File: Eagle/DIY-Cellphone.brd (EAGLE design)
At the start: 87 x 44.5 mm, 47 parts, among them IC1 MEGA1284, J1 ISP, U1 MCP73831, U7 M10_HDWITHOUT_EXCLUSION, X1 BU-SMA-V, X3 CCM03-3002 R102

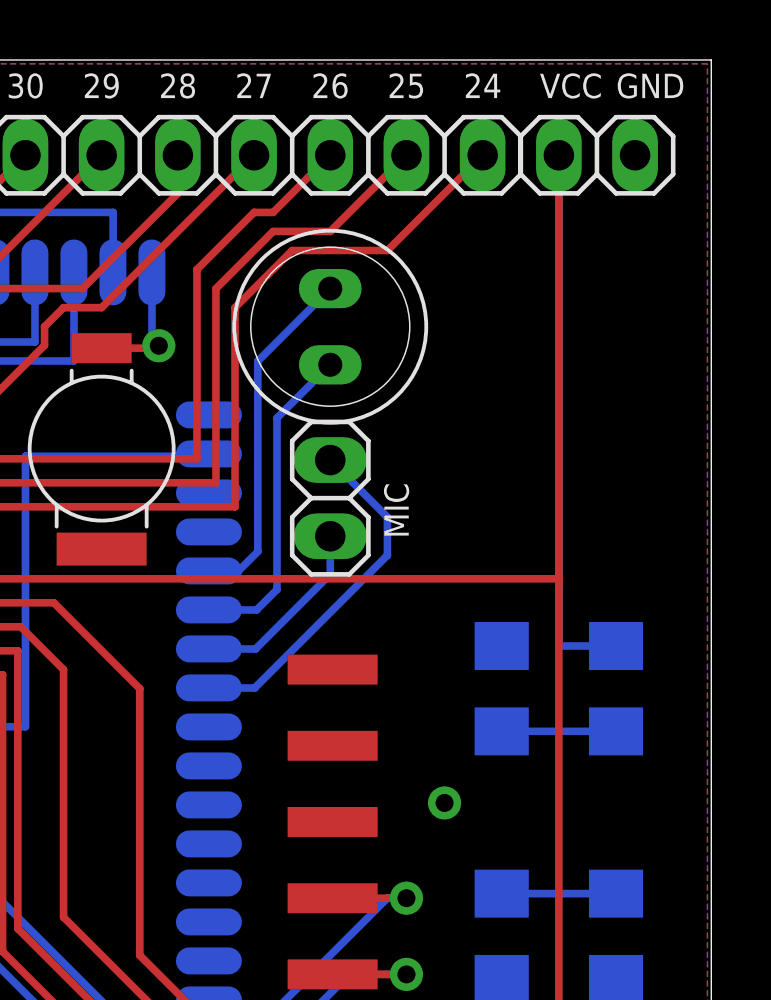
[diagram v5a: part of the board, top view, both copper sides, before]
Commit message: Move speaker and mic to edge of board.
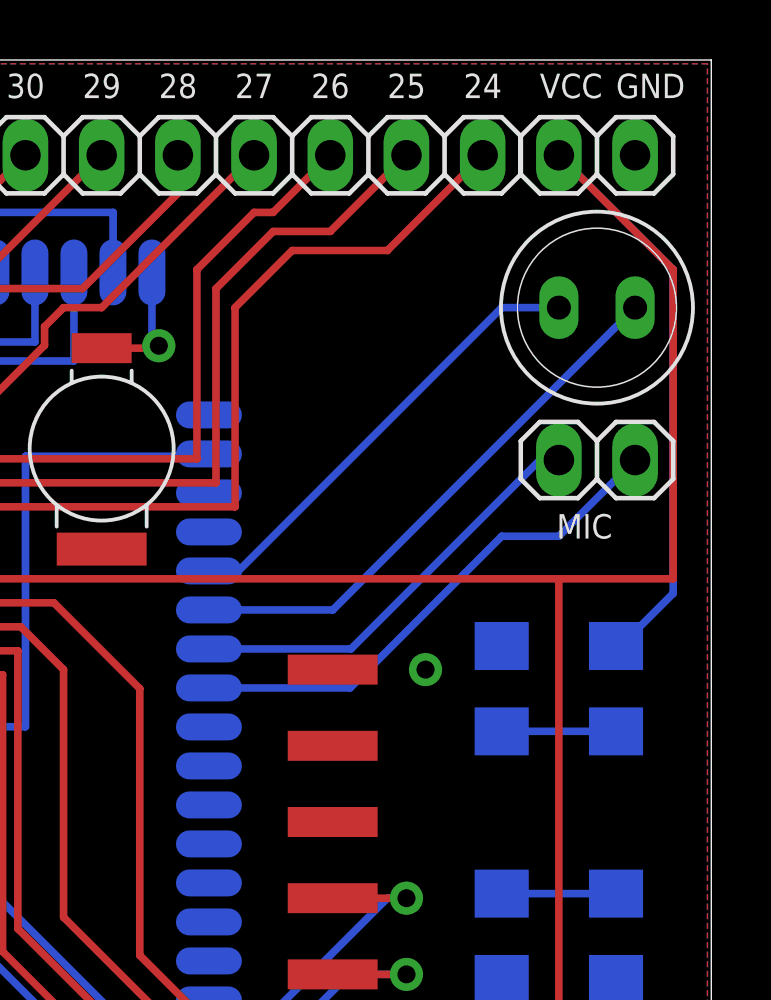
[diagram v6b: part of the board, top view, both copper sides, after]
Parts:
- moved MIC 8.98 mm to (83.2, 31.1), turned to 0 degrees
- moved SPEAKER 8.91 mm to (83.2, 36.2), turned to 0 degrees
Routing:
- net MIC1P: track 6.34 -> 14.3 mm
- net SPK1P: track 10.8 -> 18.4 mm
- net VCC: track 205.2 -> 211.2 mm
- net MIC1N: track 11.7 -> 17.4 mm
- net SPK1N: track 11.7 -> 15.3 mm
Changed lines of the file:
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@@
 <attribute name="VALUE" x="32.493" y="14.003" size="0.8128" layer="28" rot="MR90"/>
 </element>
-<element name="SPEAKER" library="cellphone" package="SPEAKER-6.4MM" value="MINI-SIREN" x="74.295" y="35.56" smashed="yes" rot="R270"/>
+<element name="SPEAKER" library="cellphone" package="SPEAKER-6.4MM" value="MINI-SIREN" x="83.185" y="36.195" smashed="yes"/>
 <element name="RST" library="cellphone" package="B3U-1000P" value="BUTTON" x="36.322" y="28.194" smashed="yes" rot="MR180">
 <attribute name="NAME" x="34.036" y="29.21" size="0.8128" layer="26" rot="MR270"/>
@@
 <attribute name="VALUE" x="39.497" y="26.543" size="0.8128" layer="28" rot="MR270"/>
 </element>
-<element name="MIC" library="pinhead" package="1X02" value="" x="74.295" y="29.845" smashed="yes" rot="R90">
-<attribute name="NAME" x="76.9112" y="28.4988" size="0.8128" layer="25" ratio="10" rot="R90"/>
-<attribute name="VALUE" x="77.47" y="27.305" size="1.27" layer="27" rot="R90"/>
+<element name="MIC" library="pinhead" package="1X02" value="" x="83.185" y="31.115" smashed="yes">
+<attribute name="NAME" x="81.8388" y="28.4988" size="0.8128" layer="25" ratio="10"/>
+<attribute name="VALUE" x="80.645" y="27.94" size="1.27" layer="27"/>
 </element>
 <element name="JP2" library="pinhead" package="1X08" value="" x="70.485" y="41.275" smashed="yes">
@@
 <contactref element="JP9" pad="1"/>
 <wire x1="61.788" y1="27.156" x2="81.915" y2="27.156" width="0.254" layer="1"/>
-<wire x1="81.915" y1="27.156" x2="81.915" y2="41.275" width="0.254" layer="1"/>
 <wire x1="81.915" y1="3.175" x2="81.915" y2="27.156" width="0.254" layer="1"/>
 <contactref element="LED3" pad="A"/>
-<wire x1="83.82" y1="24.917" x2="81.915" y2="24.917" width="0.254" layer="16"/>
-<wire x1="81.915" y1="24.917" x2="81.915" y2="41.275" width="0.254" layer="16"/>
+<wire x1="81.915" y1="41.275" x2="85.725" y2="37.465" width="0.254" layer="16"/>
+<wire x1="85.725" y1="37.465" x2="85.725" y2="26.67" width="0.254" layer="16"/>
+<wire x1="85.725" y1="26.67" x2="83.972" y2="24.917" width="0.254" layer="16"/>
+<wire x1="83.972" y1="24.917" x2="83.82" y2="24.917" width="0.254" layer="16"/>
+<wire x1="81.915" y1="27.156" x2="85.725" y2="27.156" width="0.254" layer="1"/>
+<wire x1="85.725" y1="27.156" x2="85.725" y2="37.465" width="0.254" layer="1"/>
+<wire x1="85.725" y1="37.465" x2="81.915" y2="41.275" width="0.254" layer="1"/>
 </signal>
 <signal name="ANT" class="4">
@@
 <contactref element="JP8" pad="2"/>
 <contactref element="JP9" pad="2"/>
-<via x="78.105" y="19.685" extent="1-16" drill="0.6"/>
+<via x="77.47" y="24.13" extent="1-16" drill="0.6"/>
 <contactref element="R1" pad="1"/>
 <contactref element="R5" pad="1"/>
@@
 <contactref element="SPEAKER" pad="P$1"/>
 <wire x1="70.25" y1="27.419" x2="71.234" y2="27.419" width="0.254" layer="16"/>
-<wire x1="71.234" y1="27.419" x2="71.882" y2="28.067" width="0.254" layer="16"/>
-<wire x1="71.882" y1="28.067" x2="71.882" y2="34.417" width="0.254" layer="16"/>
-<wire x1="71.882" y1="34.417" x2="74.295" y2="36.83" width="0.254" layer="16"/>
+<wire x1="71.234" y1="27.419" x2="80.01" y2="36.195" width="0.254" layer="16"/>
+<wire x1="80.01" y1="36.195" x2="81.915" y2="36.195" width="0.254" layer="16"/>
 </signal>
 <signal name="SPK1P">
 <contactref element="U7" pad="P$22"/>
 <contactref element="SPEAKER" pad="P$2"/>
-<wire x1="70.25" y1="26.119" x2="71.839" y2="26.119" width="0.254" layer="16"/>
-<wire x1="71.839" y1="26.119" x2="72.517" y2="26.797" width="0.254" layer="16"/>
-<wire x1="72.517" y1="26.797" x2="72.517" y2="32.512" width="0.254" layer="16"/>
-<wire x1="72.517" y1="32.512" x2="74.295" y2="34.29" width="0.254" layer="16"/>
+<wire x1="70.25" y1="26.119" x2="74.379" y2="26.119" width="0.254" layer="16"/>
+<wire x1="74.379" y1="26.119" x2="84.455" y2="36.195" width="0.254" layer="16"/>
 </signal>
 <signal name="MIC1N">
 <contactref element="U7" pad="P$24"/>
 <contactref element="MIC" pad="2"/>
-<wire x1="70.25" y1="23.519" x2="71.779" y2="23.519" width="0.254" layer="16"/>
-<wire x1="71.779" y1="23.519" x2="76.2" y2="27.94" width="0.254" layer="16"/>
-<wire x1="76.2" y1="27.94" x2="76.2" y2="29.21" width="0.254" layer="16"/>
-<wire x1="76.2" y1="29.21" x2="74.295" y2="31.115" width="0.254" layer="16"/>
+<wire x1="70.25" y1="23.519" x2="74.954" y2="23.519" width="0.254" layer="16"/>
+<wire x1="74.954" y1="23.519" x2="80.01" y2="28.575" width="0.254" layer="16"/>
+<wire x1="80.01" y1="28.575" x2="81.915" y2="28.575" width="0.254" layer="16"/>
+<wire x1="81.915" y1="28.575" x2="84.455" y2="31.115" width="0.254" layer="16"/>
 </signal>
 <signal name="MIC2P">
@@
 <contactref element="U7" pad="P$23"/>
 <contactref element="MIC" pad="1"/>
-<wire x1="70.25" y1="24.819" x2="71.809" y2="24.819" width="0.254" layer="16"/>
-<wire x1="71.809" y1="24.819" x2="74.295" y2="27.305" width="0.254" layer="16"/>
-<wire x1="74.295" y1="27.305" x2="74.295" y2="28.575" width="0.254" layer="16"/>
+<wire x1="70.25" y1="24.819" x2="74.984" y2="24.819" width="0.254" layer="16"/>
+<wire x1="74.984" y1="24.819" x2="81.28" y2="31.115" width="0.254" layer="16"/>
+<wire x1="81.28" y1="31.115" x2="81.915" y2="31.115" width="0.254" layer="16"/>
 </signal>
 <signal name="KBC0">

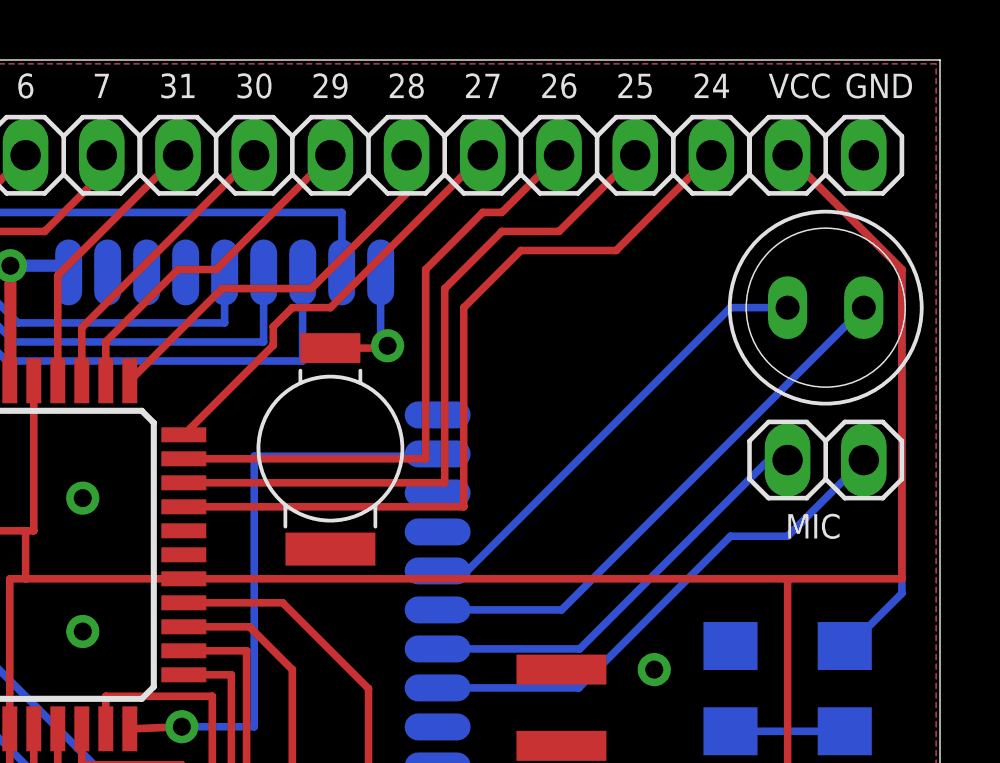
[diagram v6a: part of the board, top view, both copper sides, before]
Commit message: Connect airwire.
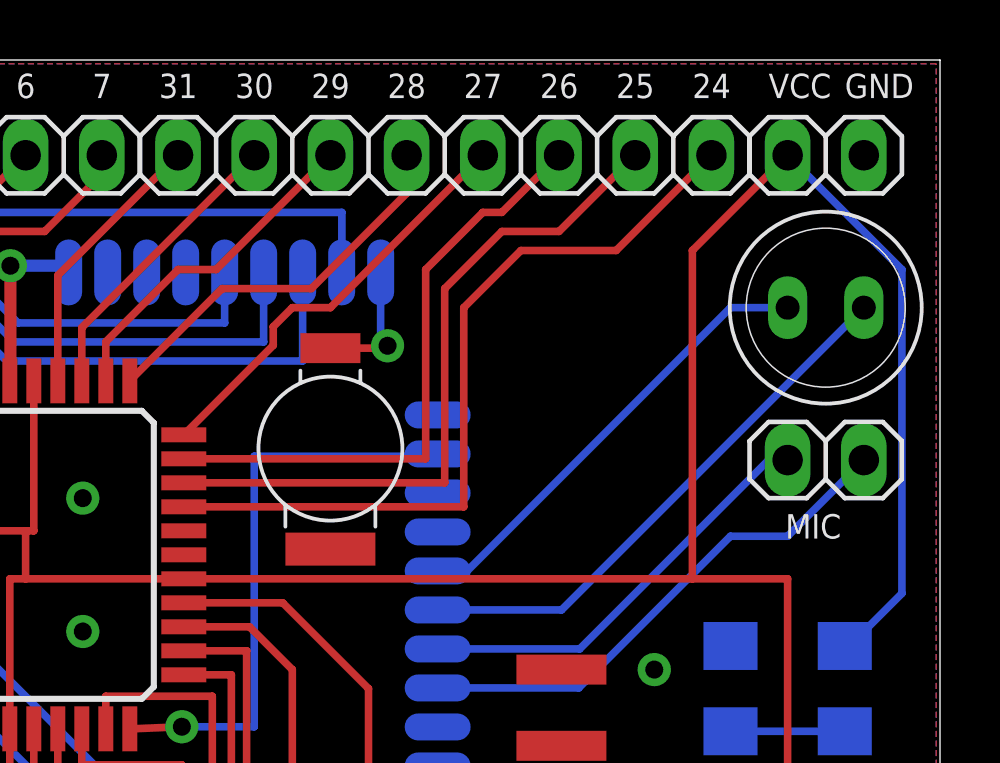
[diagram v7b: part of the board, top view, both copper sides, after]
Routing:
- net VCC: track 211.2 -> 207.1 mm
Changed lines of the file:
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@@
 <contactref element="JP8" pad="1"/>
 <contactref element="JP9" pad="1"/>
-<wire x1="61.788" y1="27.156" x2="81.915" y2="27.156" width="0.254" layer="1"/>
+<wire x1="61.788" y1="27.156" x2="78.74" y2="27.156" width="0.254" layer="1"/>
+<wire x1="78.74" y1="27.156" x2="81.915" y2="27.156" width="0.254" layer="1"/>
 <wire x1="81.915" y1="3.175" x2="81.915" y2="27.156" width="0.254" layer="1"/>
 <contactref element="LED3" pad="A"/>
@@
 <wire x1="85.725" y1="26.67" x2="83.972" y2="24.917" width="0.254" layer="16"/>
 <wire x1="83.972" y1="24.917" x2="83.82" y2="24.917" width="0.254" layer="16"/>
-<wire x1="81.915" y1="27.156" x2="85.725" y2="27.156" width="0.254" layer="1"/>
-<wire x1="85.725" y1="27.156" x2="85.725" y2="37.465" width="0.254" layer="1"/>
-<wire x1="85.725" y1="37.465" x2="81.915" y2="41.275" width="0.254" layer="1"/>
+<wire x1="81.915" y1="41.275" x2="78.74" y2="38.1" width="0.254" layer="1"/>
+<wire x1="78.74" y1="38.1" x2="78.74" y2="27.156" width="0.254" layer="1"/>
 </signal>
 <signal name="ANT" class="4">
